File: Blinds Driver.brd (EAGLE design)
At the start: 72.1 x 61 mm, 29 parts

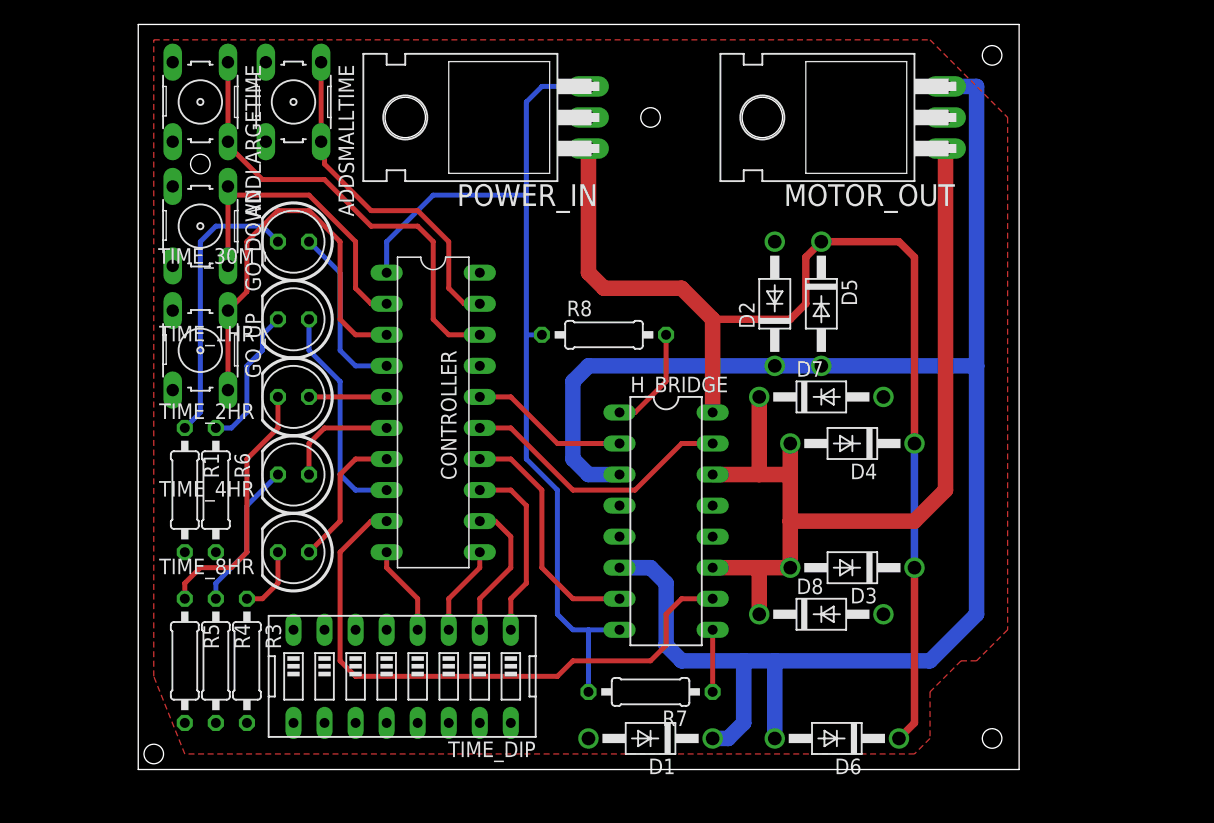
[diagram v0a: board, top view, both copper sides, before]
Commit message: Fit into smaller PCB! Use 4-pin DIP
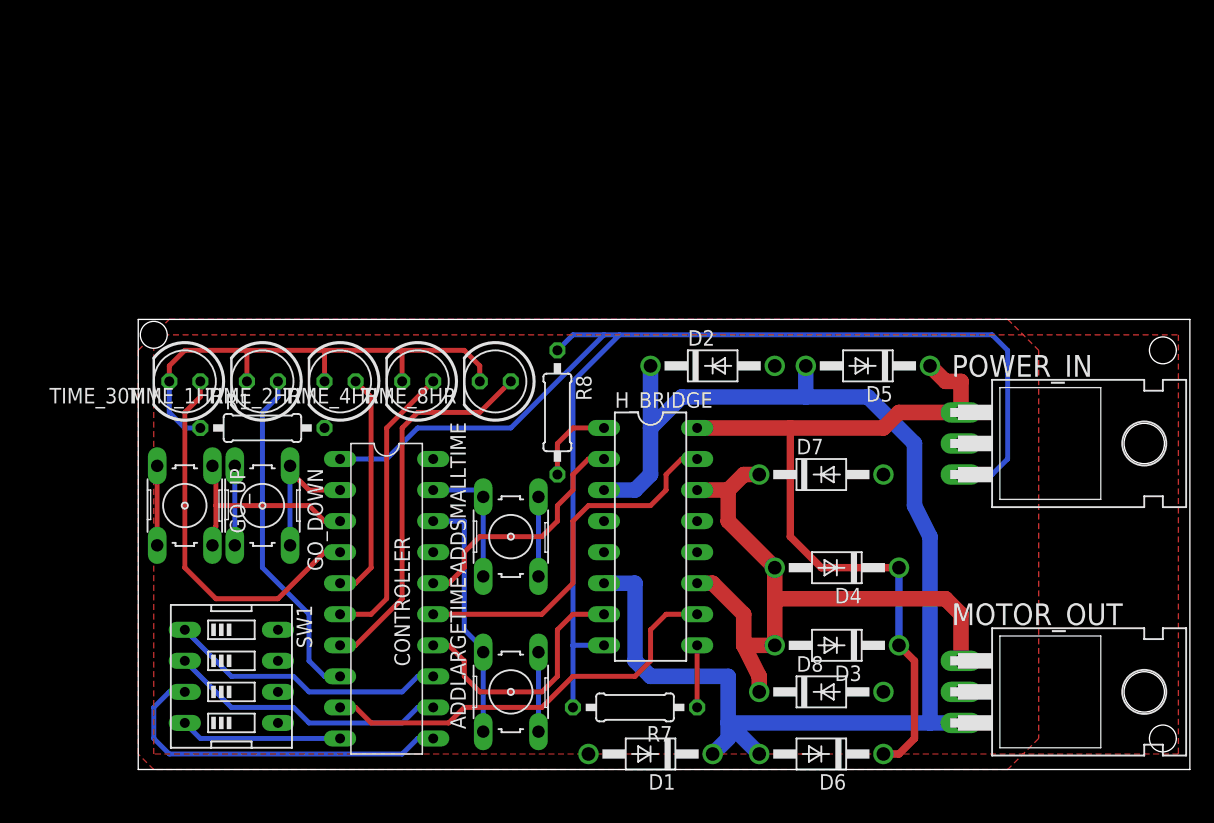
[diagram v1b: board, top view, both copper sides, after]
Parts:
- removed R3, R4, R5, R6: (no value), resistor:0207/10
- removed TIME_DIP: (no value), special:EDG-08
- added SW1: (no value), special:EDG-04
- moved POWER_IN 57.4 mm to (90.2, 39.4), turned to 270 degrees
- moved ADDLARGETIME 54.5 mm to (43.2, 19.1), turned to 90 degrees
- moved MOTOR_OUT 51.7 mm to (90.2, 19.1), turned to 270 degrees
- moved ADDSMALLTIME 39.8 mm to (43.2, 31.8), turned to 90 degrees
- moved GO_DOWN 23.4 mm to (22.9, 34.3)
- moved TIME_8HR 21.6 mm to (41.9, 44.5)
- moved CONTROLLER 15.7 mm to (33.0, 26.7)
- moved TIME_30M 14.5 mm to (16.5, 44.5)
- moved GO_UP 12.8 mm to (16.5, 34.3)
- moved TIME_4HR 12.7 mm to (35.6, 44.5)
- moved D4 10.2 mm to (69.8, 29.2)
- moved R1 8.13 mm to (22.9, 40.6), turned to 0 degrees
- moved R8 7.41 mm to (47.0, 41.9), turned to 270 degrees
- moved D2 7.18 mm to (59.7, 45.7), turned to 0 degrees
- moved D3 6.48 mm to (69.8, 22.9)
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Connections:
- removed net N$15: R4.1, TIME_4HR.K
- removed net N$16: R5.1, TIME_2HR.K
- removed net N$17: R6.1, TIME_1HR.K
- removed net N$23: R1.1, TIME_30M.K
- net GND: now also SW1.5, SW1.6, SW1.7, SW1.8; no longer R3.2, R4.2, R5.2, R6.2, TIME_DIP.13, TIME_DIP.14, TIME_DIP.15, TIME_DIP.16
- net N$14: now also R1.1, TIME_1HR.K, TIME_2HR.K, TIME_30M.K, TIME_4HR.K; no longer R3.1
- net N$4: now also SW1.1; no longer TIME_DIP.1
- net N$5: now also SW1.2; no longer TIME_DIP.2
- net N$7: now also SW1.3; no longer TIME_DIP.3
- net N$9: now also SW1.4; no longer TIME_DIP.4
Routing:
- net N$14: track 5.61 -> 42.2 mm
- net +5V: track 76.1 -> 111.5 mm
- net N$25: track 141.4 -> 109.7 mm
- net +12V: track 91.3 -> 64.1 mm
- net GND: track 0.00 -> 26.0 mm
- net N$23: track 23.2 -> 0.00 mm
- net N$7: track 7.40 -> 29.5 mm
- net N$28: track 74.7 -> 53.5 mm
- net N$16: track 21.2 -> 0.00 mm
- net N$10: track 11.7 -> 31.1 mm
- net N$18: track 28.1 -> 11.0 mm
- net N$24: track 14.3 -> 31.1 mm
- net N$19: track 37.5 -> 21.1 mm
- net N$20: track 33.2 -> 17.3 mm
- net N$11: track 9.42 -> 23.7 mm
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- added copper zone on layer 1, net GND
- removed copper zone on layer 1, net N$26
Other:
- board size 72.1 x 61 mm -> 86 x 36.8 mm

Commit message: Improve clearances
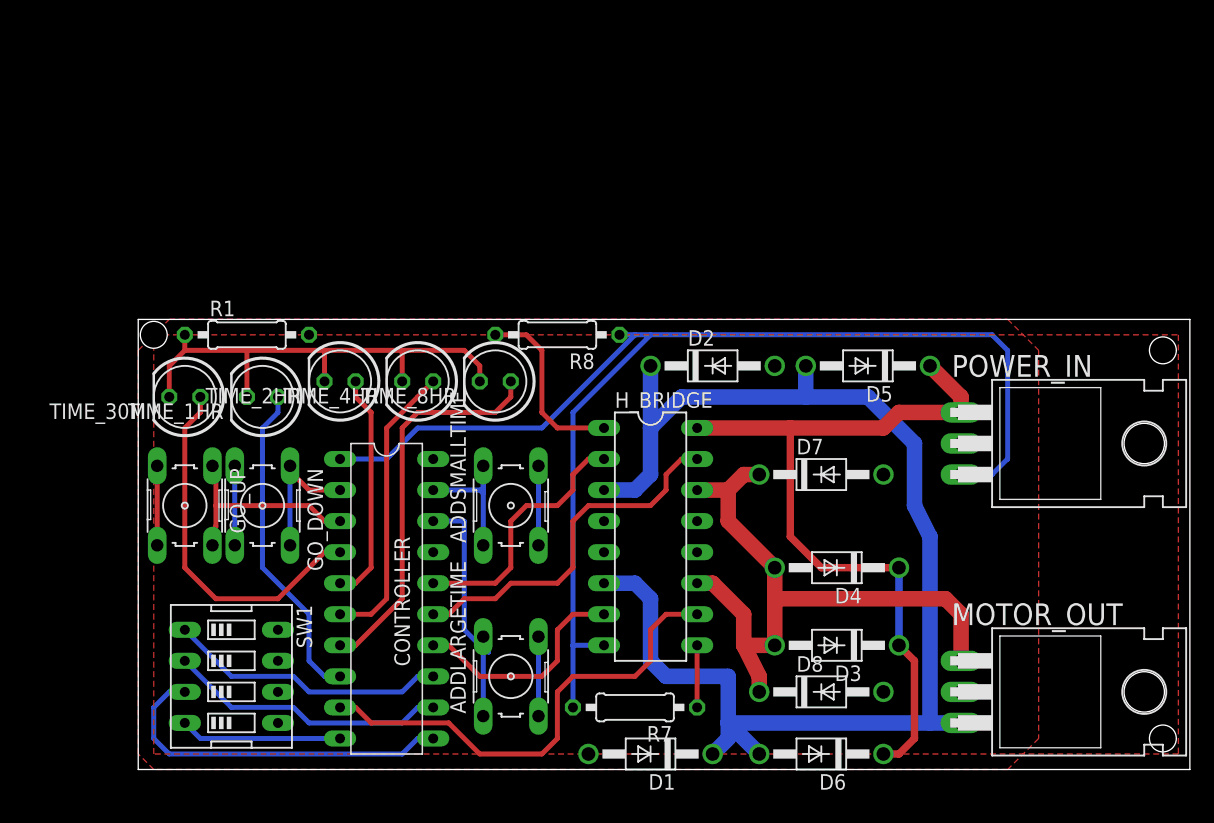
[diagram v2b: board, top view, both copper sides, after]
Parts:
- moved R1 7.73 mm to (21.6, 48.3)
- moved R8 6.35 mm to (47.0, 48.3), turned to 180 degrees
- moved ADDSMALLTIME 2.54 mm to (43.2, 34.3)
- moved TIME_1HR 1.27 mm to (22.9, 43.2)
- moved TIME_30M 1.27 mm to (16.5, 43.2)
- moved ADDLARGETIME 1.27 mm to (43.2, 20.3)
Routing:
- net N$6: track 6.88 -> 15.0 mm
- net N$22: track 34.9 -> 39.2 mm
- net N$2: track 21.2 -> 18.6 mm
- net +5V: track 111.5 -> 109.5 mm
- net N$18: track 11.0 -> 13.0 mm
- net N$21: track 13.6 -> 11.7 mm
- net N$14: track 42.2 -> 40.4 mm
- net N$24: track 31.1 -> 29.8 mm
- net N$13: track 28.0 -> 26.8 mm
- net N$19: track 21.1 -> 22.0 mm
- net N$3: track 30.6 -> 29.8 mm
- net N$10: track 31.1 -> 31.8 mm
- net N$1: track 20.4 -> 21.2 mm
- net +12V: track 64.1 -> 63.4 mm
- net N$25: track 109.7 -> 109.0 mm

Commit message: More tweaks
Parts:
- moved R8 1.27 mm to (45.7, 48.3)
- moved TIME_2HR 1.27 mm to (29.2, 43.2)
- moved TIME_4HR 1.27 mm to (35.6, 43.2)
- moved TIME_8HR 1.27 mm to (41.9, 43.2)
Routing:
- net N$25: track 109.0 -> 115.6 mm
- net +5V: track 109.5 -> 103.1 mm
- net N$14: track 40.4 -> 44.2 mm
- net N$19: track 22.0 -> 19.7 mm
- net N$12: track 18.8 -> 17.6 mm
- net N$11: track 23.7 -> 22.4 mm
- net N$10: track 31.8 -> 30.6 mm
- net N$6: track 15.0 -> 16.3 mm
- net N$3: track 29.8 -> 29.1 mm
- net N$1: track 21.2 -> 20.4 mm

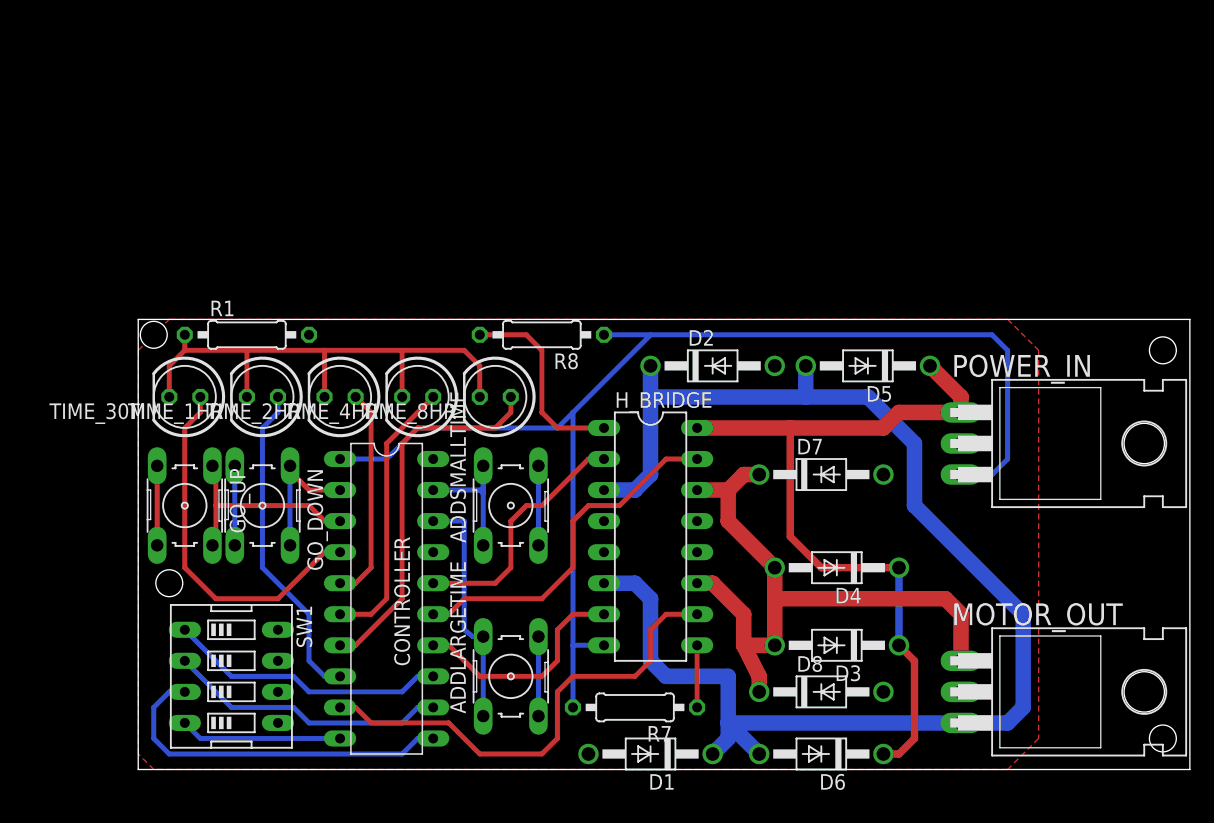
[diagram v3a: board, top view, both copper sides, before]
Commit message: 1) Diodes were doubled up 2) Only one half-bridge is needed 3) VCC 2 is +12V, VCC1 is +5V 4) Added 2 bypass capacitors on the power supply lines to stabilize power supply
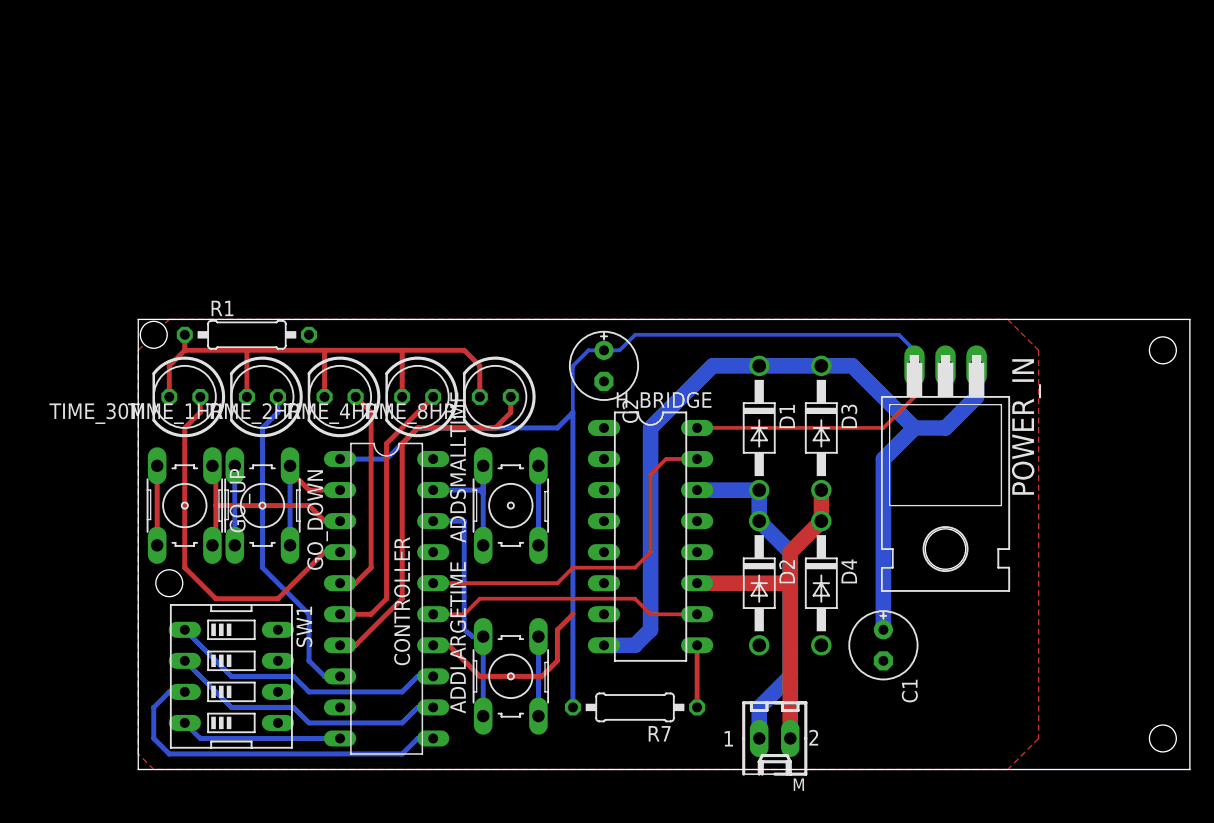
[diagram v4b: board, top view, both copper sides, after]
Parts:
- removed D5, D6, D7, D8: 1N4004, diode:DO41-10
- removed MOTOR_OUT: 7805T, linear:TO220H
- removed R8: (no value), resistor:0207/10
- added C1, C2: 1u, rcl:E2,5-6E
- added M: 22-27-2021-02, con-molex:6410-02
- moved D1 28.1 mm to (63.5, 40.6), turned to 270 degrees
- moved D2 18.2 mm to (63.5, 27.9), turned to 270 degrees
- moved D3 17.8 mm to (68.6, 40.6), turned to 270 degrees
- moved POWER_IN 12.0 mm to (78.7, 35.6), turned to 180 degrees
- moved D4 1.80 mm to (68.6, 27.9), turned to 270 degrees
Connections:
- removed net N$1: CONTROLLER.16, H_BRIDGE.2
- removed net N$22: CONTROLLER.9, H_BRIDGE.10
- removed net N$25: D1.C, D2.C, D5.A, D6.A, H_BRIDGE.3, H_BRIDGE.6, MOTOR_OUT.3
- removed net N$28: D3.A, D4.A, D7.C, D8.C, H_BRIDGE.11, H_BRIDGE.14, MOTOR_OUT.1
- new net M1CONTROL: CONTROLLER.16, H_BRIDGE.15
- new net M2CONTROL: CONTROLLER.15, H_BRIDGE.10
- net +12V: now also C1.+, D1.C, H_BRIDGE.8; no longer D4.C, D5.C, D6.C, H_BRIDGE.16
- net +5V: now also C2.+, H_BRIDGE.16; no longer H_BRIDGE.8, R8.1
- net GND: now also C1.-, C2.-, D4.A, H_BRIDGE.1, H_BRIDGE.2, H_BRIDGE.7; no longer D1.A, D7.A, D8.A
- net N$2: no longer H_BRIDGE.7
- net N$3: now also D1.A, D2.C, H_BRIDGE.14, M.1; no longer CONTROLLER.15, H_BRIDGE.15
- net N$6: now also D3.A, D4.C, H_BRIDGE.11, M.2; no longer H_BRIDGE.1, R8.2
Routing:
- net N$25: track 115.6 -> 0.00 mm
- net N$28: track 53.5 -> 0.00 mm
- net N$22: track 39.2 -> 0.00 mm
- net M1CONTROL: track 0.00 -> 29.5 mm
- net M2CONTROL: track 0.00 -> 22.6 mm
- net N$1: track 20.4 -> 0.00 mm
- net N$6: track 16.3 -> 29.0 mm
- net +12V: track 63.4 -> 72.9 mm
- net N$2: track 18.6 -> 16.1 mm
- net +5V: track 103.1 -> 100.7 mm
- net N$3: track 29.1 -> 27.5 mm

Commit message: Pin A3 is input-only, so use C7 instead
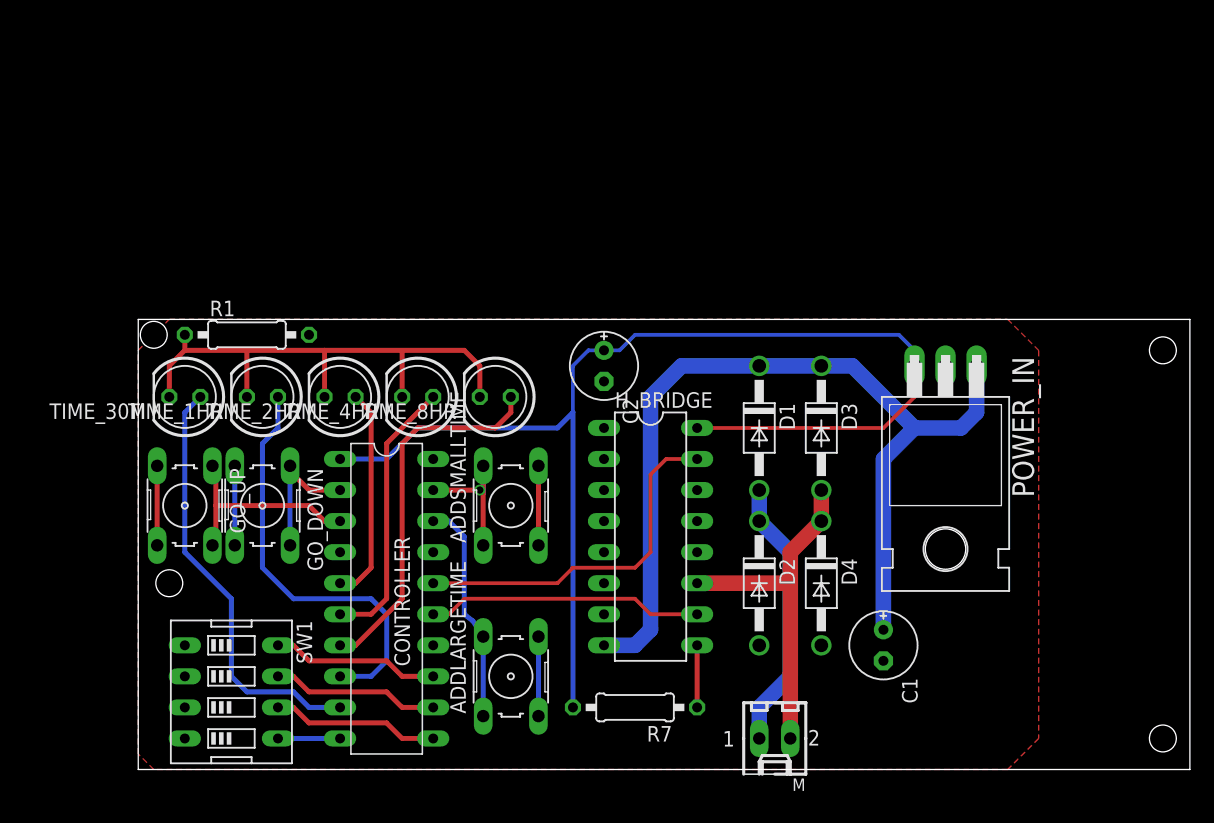
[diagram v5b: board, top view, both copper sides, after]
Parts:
- moved SW1 1.27 mm to (20.3, 19.1)
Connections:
- removed net N$2: CONTROLLER.14
- removed net N$9: CONTROLLER.10, SW1.4
- new net N$1: CONTROLLER.10, SW1.5
- net GND: now also CONTROLLER.14, CONTROLLER.17, CONTROLLER.4, SW1.1, SW1.2, SW1.3, SW1.4; no longer SW1.5, SW1.6, SW1.7, SW1.8
- net N$24: now also CONTROLLER.9; no longer CONTROLLER.4
- net N$4: now also CONTROLLER.11, SW1.6; no longer CONTROLLER.13, SW1.1
- net N$5: now also SW1.7; no longer SW1.2
- net N$7: now also CONTROLLER.13, SW1.8; no longer CONTROLLER.11, SW1.3
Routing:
- net N$2: track 16.1 -> 0.00 mm
- net N$7: track 29.5 -> 13.8 mm
- net N$9: track 13.2 -> 0.00 mm
- net N$5: track 23.0 -> 13.8 mm
- net N$4: track 23.0 -> 13.8 mm
- net N$13: track 26.8 -> 34.4 mm
- net N$24: track 29.8 -> 34.9 mm
- net N$1: track 0.00 -> 5.08 mm
- net N$3: track 27.5 -> 22.4 mm
- net +12V: track 72.9 -> 75.1 mm
- net N$19: track 19.7 -> 18.3 mm
- net N$18: vias 0 -> 1
